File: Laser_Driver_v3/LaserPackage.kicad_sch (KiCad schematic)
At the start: 16 parts

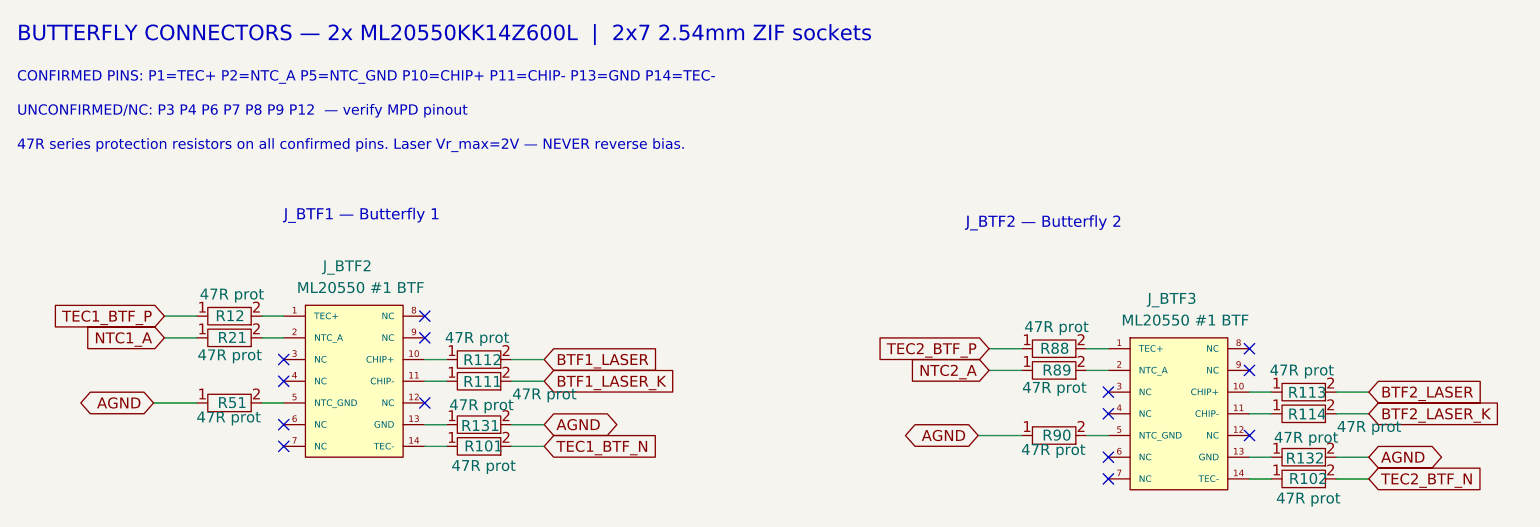
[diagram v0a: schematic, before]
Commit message: Renumbered schematics, corrections, power verified
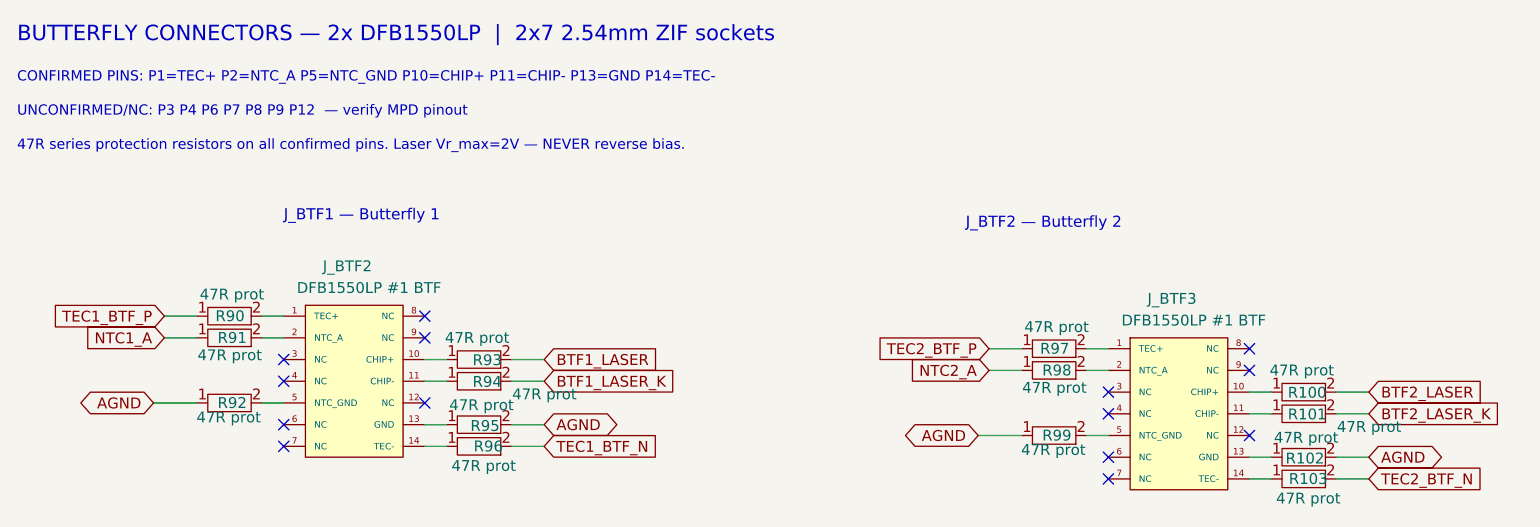
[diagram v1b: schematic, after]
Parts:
- J_BTF2, J_BTF3: value ML20550 #1 BTF -> DFB1550LP #1 BTF
- renumbered R113 to R100, R114 to R101, R132 to R102, R102 to R103, R12 to R90, R21 to R91, R51 to R92, R112 to R93, R111 to R94, R131 to R95, R101 to R96, R88 to R97, R89 to R98, R90 to R99
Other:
- note added: "BUTTERFLY CONNECTORS — 2x DFB1550LP | 2x7 2.54mm ZIF sockets"
- note removed: "BUTTERFLY CONNECTORS — 2x ML20550KK14Z600L | 2x7 2.54mm ZIF sockets"
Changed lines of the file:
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@@
 		)
 	)
-	(text "BUTTERFLY CONNECTORS — 2x ML20550KK14Z600L  |  2x7 2.54mm ZIF sockets"
+	(text "BUTTERFLY CONNECTORS — 2x DFB1550LP  |  2x7 2.54mm ZIF sockets"
 		(exclude_from_sim no)
 		(at 41.18 30.61 0)
@@
 			)
 		)
-		(property "Value" "ML20550 #1 BTF"
+		(property "Value" "DFB1550LP #1 BTF"
 			(at 170.434 64.008 0)
 			(show_name no)
@@
 		(in_pos_files yes)
 		(dnp no)
-		(property "Reference" "R113"
+		(property "Reference" "R100"
 			(at 194.438 72.456 90)
 			(show_name no)
@@
 			(project "laser_driver_v3"
 				(path "/b2c3d4e5-f6a7-8901-bcde-f12345678901/3cc9b630-4516-4d07-8624-99717cc6cbce"
-					(reference "R113")
+					(reference "R100")
 					(unit 1)
 				)
@@
 		(in_pos_files yes)
 		(dnp no)
-		(property "Reference" "R12"
+		(property "Reference" "R90"
 			(at 67.818 63.5 90)
 			(show_name no)
@@
 			(project "laser_driver_v3"
 				(path "/b2c3d4e5-f6a7-8901-bcde-f12345678901/3cc9b630-4516-4d07-8624-99717cc6cbce"
-					(reference "R12")
+					(reference "R90")
 					(unit 1)
 				)
@@
 		(in_pos_files yes)
 		(dnp no)
-		(property "Reference" "R132"
+		(property "Reference" "R102"
 			(at 194.184 80.156 90)
 			(show_name no)
@@
 			(project "laser_driver_v3"
 				(path "/b2c3d4e5-f6a7-8901-bcde-f12345678901/3cc9b630-4516-4d07-8624-99717cc6cbce"
-					(reference "R132")
+					(reference "R102")
 					(unit 1)
 				)
@@
 		(in_pos_files yes)
 		(dnp no)
-		(property "Reference" "R131"
+		(property "Reference" "R95"
 			(at 97.664 76.346 90)
 			(show_name no)
@@
 			(project "laser_driver_v3"
 				(path "/b2c3d4e5-f6a7-8901-bcde-f12345678901/3cc9b630-4516-4d07-8624-99717cc6cbce"
-					(reference "R131")
+					(reference "R95")
 					(unit 1)
 				)
@@
 		(in_pos_files yes)
 		(dnp no)
-		(property "Reference" "R21"
+		(property "Reference" "R91"
 			(at 68.072 66.04 90)
 			(show_name no)
@@
 			(project "laser_driver_v3"
 				(path "/b2c3d4e5-f6a7-8901-bcde-f12345678901/3cc9b630-4516-4d07-8624-99717cc6cbce"
-					(reference "R21")
+					(reference "R91")
 					(unit 1)
 				)
@@
 		(in_pos_files yes)
 		(dnp no)
-		(property "Reference" "R112"
+		(property "Reference" "R93"
 			(at 97.918 68.646 90)
 			(show_name no)
@@
 			(project "laser_driver_v3"
 				(path "/b2c3d4e5-f6a7-8901-bcde-f12345678901/3cc9b630-4516-4d07-8624-99717cc6cbce"
-					(reference "R112")
+					(reference "R93")
 					(unit 1)
 				)
@@
 		(in_pos_files yes)
 		(dnp no)
-		(property "Reference" "R88"
+		(property "Reference" "R97"
 			(at 164.338 67.31 90)
 			(show_name no)
@@
 			(project "laser_driver_v3"
 				(path "/b2c3d4e5-f6a7-8901-bcde-f12345678901/3cc9b630-4516-4d07-8624-99717cc6cbce"
-					(reference "R88")
+					(reference "R97")
 					(unit 1)
 				)
@@
 		(in_pos_files yes)
 		(dnp no)
-		(property "Reference" "R101"
+		(property "Reference" "R96"
 			(at 98.044 78.74 90)
 			(show_name no)
@@
 			(project "laser_driver_v3"
 				(path "/b2c3d4e5-f6a7-8901-bcde-f12345678901/3cc9b630-4516-4d07-8624-99717cc6cbce"
-					(reference "R101")
+					(reference "R96")
 					(unit 1)
 				)
@@
 		(in_pos_files yes)
 		(dnp no)
-		(property "Reference" "R114"
+		(property "Reference" "R101"
 			(at 194.438 74.996 90)
 			(show_name no)
@@
 			(project "laser_driver_v3"
 				(path "/b2c3d4e5-f6a7-8901-bcde-f12345678901/3cc9b630-4516-4d07-8624-99717cc6cbce"
-					(reference "R114")
+					(reference "R101")
 					(unit 1)
 				)
@@
 			)
 		)
-		(property "Value" "ML20550 #1 BTF"
+		(property "Value" "DFB1550LP #1 BTF"
 			(at 73.914 60.198 0)
 			(show_name no)
@@
 		(in_pos_files yes)
 		(dnp no)
-		(property "Reference" "R89"
+		(property "Reference" "R98"
 			(at 164.592 69.85 90)
 			(show_name no)
@@
 			(project "laser_driver_v3"
 				(path "/b2c3d4e5-f6a7-8901-bcde-f12345678901/3cc9b630-4516-4d07-8624-99717cc6cbce"
-					(reference "R89")
+					(reference "R98")
 					(unit 1)
 				)
@@
 		(in_pos_files yes)
 		(dnp no)
-		(property "Reference" "R90"
+		(property "Reference" "R99"
 			(at 164.592 77.47 90)
 			(show_name no)
@@
 			(project "laser_driver_v3"
 				(path "/b2c3d4e5-f6a7-8901-bcde-f12345678901/3cc9b630-4516-4d07-8624-99717cc6cbce"
-					(reference "R90")
+					(reference "R99")
 					(unit 1)
 				)
@@
 		(in_pos_files yes)
 		(dnp no)
-		(property "Reference" "R111"
+		(property "Reference" "R94"
 			(at 97.918 71.186 90)
 			(show_name no)
@@
 			(project "laser_driver_v3"
 				(path "/b2c3d4e5-f6a7-8901-bcde-f12345678901/3cc9b630-4516-4d07-8624-99717cc6cbce"
-					(reference "R111")
+					(reference "R94")
 					(unit 1)
 				)
@@
 		(in_pos_files yes)
 		(dnp no)
-		(property "Reference" "R102"
+		(property "Reference" "R103"
 			(at 194.564 82.55 90)
 			(show_name no)
@@
 			(project "laser_driver_v3"
 				(path "/b2c3d4e5-f6a7-8901-bcde-f12345678901/3cc9b630-4516-4d07-8624-99717cc6cbce"
-					(reference "R102")
+					(reference "R103")
 					(unit 1)
 				)
@@
 		(in_pos_files yes)
 		(dnp no)
-		(property "Reference" "R51"
+		(property "Reference" "R92"
 			(at 68.072 73.66 90)
 			(show_name no)
@@
 			(project "laser_driver_v3"
 				(path "/b2c3d4e5-f6a7-8901-bcde-f12345678901/3cc9b630-4516-4d07-8624-99717cc6cbce"
-					(reference "R51")
+					(reference "R92")
 					(unit 1)
 				)

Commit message: Update names, footprints, values, and created BOM
Updated files names, foot prints, component values, parts.
Assigned values from Digikey catalog.
Created CSV BOMs for each schematic.
Including a Power analysis now for all components.
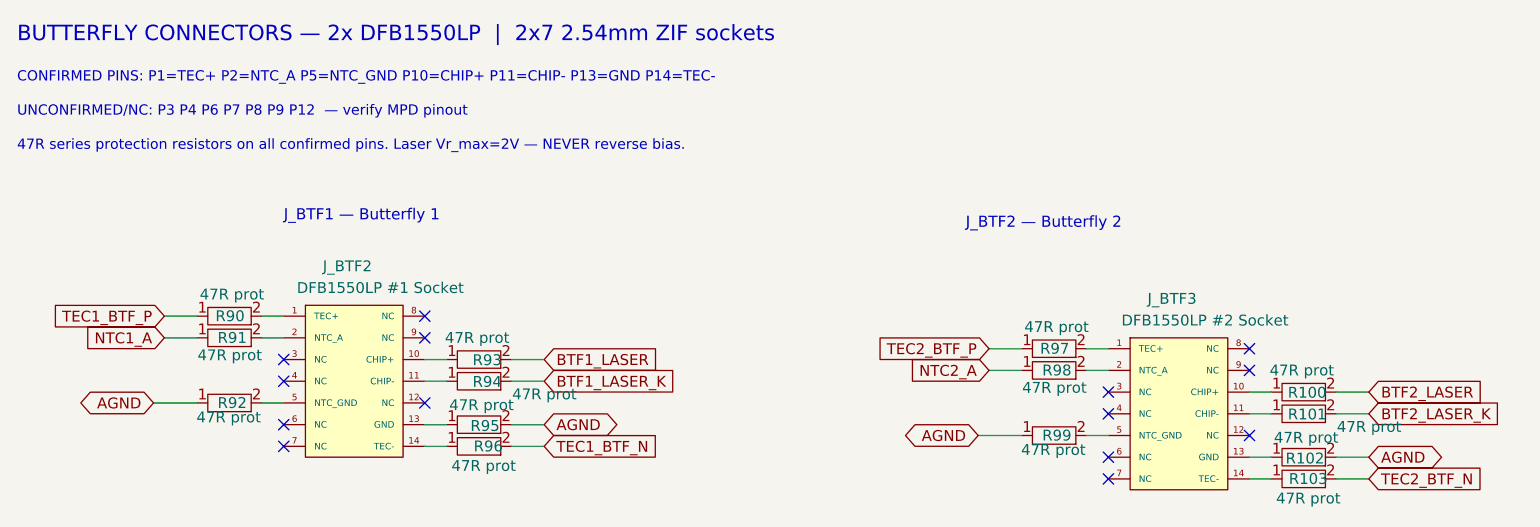
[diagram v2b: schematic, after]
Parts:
- J_BTF2: value DFB1550LP #1 BTF -> DFB1550LP #1 Socket; footprint Connector_PinHeader_2.54mm:PinHeader_2x07_P2.54mm_Vertical -> Connector_PinSocket_2.54mm:PinSocket_2x07_P2.54mm_Vertical
- J_BTF3: value DFB1550LP #1 BTF -> DFB1550LP #2 Socket; footprint Connector_PinHeader_2.54mm:PinHeader_2x07_P2.54mm_Vertical -> Connector_PinSocket_2.54mm:PinSocket_2x07_P2.54mm_Vertical
- R100, R101, R102, R103, R90, R91, R92, R93, R94, R95, R96, R97, R98, R99: footprint Resistor_SMD:R_0402_1005Metric -> Resistor_SMD:R_0805_2012Metric_Pad1.20x1.40mm_HandSolder
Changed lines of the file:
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@@
 			)
 		)
-		(property "Value" "DFB1550LP #1 BTF"
+		(property "Value" "DFB1550LP #2 Socket"
 			(at 170.434 64.008 0)
 			(show_name no)
@@
 			)
 		)
-		(property "Footprint" "Connector_PinHeader_2.54mm:PinHeader_2x07_P2.54mm_Vertical"
+		(property "Footprint" "Connector_PinSocket_2.54mm:PinSocket_2x07_P2.54mm_Vertical"
 			(at 180.594 85.598 0)
 			(hide yes)
@@
 			)
 		)
-		(property "Footprint" "Resistor_SMD:R_0402_1005Metric"
+		(property "Footprint" "Resistor_SMD:R_0805_2012Metric_Pad1.20x1.40mm_HandSolder"
 			(at 191.77 72.39 0)
 			(hide yes)
@@
 			)
 		)
-		(property "Footprint" "Resistor_SMD:R_0402_1005Metric"
+		(property "Footprint" "Resistor_SMD:R_0805_2012Metric_Pad1.20x1.40mm_HandSolder"
 			(at 66.04 63.5 0)
 			(hide yes)
@@
 			)
 		)
-		(property "Footprint" "Resistor_SMD:R_0402_1005Metric"
+		(property "Footprint" "Resistor_SMD:R_0805_2012Metric_Pad1.20x1.40mm_HandSolder"
 			(at 191.77 80.01 0)
 			(hide yes)
@@
 			)
 		)
-		(property "Footprint" "Resistor_SMD:R_0402_1005Metric"
+		(property "Footprint" "Resistor_SMD:R_0805_2012Metric_Pad1.20x1.40mm_HandSolder"
 			(at 95.25 76.2 0)
 			(hide yes)
@@
 			)
 		)
-		(property "Footprint" "Resistor_SMD:R_0402_1005Metric"
+		(property "Footprint" "Resistor_SMD:R_0805_2012Metric_Pad1.20x1.40mm_HandSolder"
 			(at 66.04 66.04 0)
 			(hide yes)
@@
 			)
 		)
-		(property "Footprint" "Resistor_SMD:R_0402_1005Metric"
+		(property "Footprint" "Resistor_SMD:R_0805_2012Metric_Pad1.20x1.40mm_HandSolder"
 			(at 95.25 68.58 0)
 			(hide yes)
@@
 			)
 		)
-		(property "Footprint" "Resistor_SMD:R_0402_1005Metric"
+		(property "Footprint" "Resistor_SMD:R_0805_2012Metric_Pad1.20x1.40mm_HandSolder"
 			(at 162.56 67.31 0)
 			(hide yes)
@@
 			)
 		)
-		(property "Footprint" "Resistor_SMD:R_0402_1005Metric"
+		(property "Footprint" "Resistor_SMD:R_0805_2012Metric_Pad1.20x1.40mm_HandSolder"
 			(at 95.25 78.74 0)
 			(hide yes)
@@
 			)
 		)
-		(property "Footprint" "Resistor_SMD:R_0402_1005Metric"
+		(property "Footprint" "Resistor_SMD:R_0805_2012Metric_Pad1.20x1.40mm_HandSolder"
 			(at 191.77 74.93 0)
 			(hide yes)
@@
 			)
 		)
-		(property "Value" "DFB1550LP #1 BTF"
+		(property "Value" "DFB1550LP #1 Socket"
 			(at 73.914 60.198 0)
 			(show_name no)
@@
 			)
 		)
-		(property "Footprint" "Connector_PinHeader_2.54mm:PinHeader_2x07_P2.54mm_Vertical"
+		(property "Footprint" "Connector_PinSocket_2.54mm:PinSocket_2x07_P2.54mm_Vertical"
 			(at 84.074 81.788 0)
 			(hide yes)
@@
 			)
 		)
-		(property "Footprint" "Resistor_SMD:R_0402_1005Metric"
+		(property "Footprint" "Resistor_SMD:R_0805_2012Metric_Pad1.20x1.40mm_HandSolder"
 			(at 162.56 69.85 0)
 			(hide yes)
@@
 			)
 		)
-		(property "Footprint" "Resistor_SMD:R_0402_1005Metric"
+		(property "Footprint" "Resistor_SMD:R_0805_2012Metric_Pad1.20x1.40mm_HandSolder"
 			(at 162.56 77.47 0)
 			(hide yes)
@@
 			)
 		)
-		(property "Footprint" "Resistor_SMD:R_0402_1005Metric"
+		(property "Footprint" "Resistor_SMD:R_0805_2012Metric_Pad1.20x1.40mm_HandSolder"
 			(at 95.25 71.12 0)
 			(hide yes)
@@
 			)
 		)
-		(property "Footprint" "Resistor_SMD:R_0402_1005Metric"
+		(property "Footprint" "Resistor_SMD:R_0805_2012Metric_Pad1.20x1.40mm_HandSolder"
 			(at 191.77 82.55 0)
 			(hide yes)
@@
 			)
 		)
-		(property "Footprint" "Resistor_SMD:R_0402_1005Metric"
+		(property "Footprint" "Resistor_SMD:R_0805_2012Metric_Pad1.20x1.40mm_HandSolder"
 			(at 66.04 73.66 0)
 			(hide yes)

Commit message: first placement of all components on pcb.
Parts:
- removed J_BTF2: DFB1550LP #1 Socket, Connector_PinSocket_2.54mm:PinSocket_2x07_P2.54mm_Vertical, symbol Connector:Conn_02x07_Odd_Even
- removed J_BTF3: DFB1550LP #2 Socket, Connector_PinSocket_2.54mm:PinSocket_2x07_P2.54mm_Vertical, symbol Connector:Conn_02x07_Odd_Even
- removed R100, R101, R102, R103, R90, R91, R92, R93, R94, R95, R96, R97, R98, R99: 47R prot, Resistor_SMD:R_0805_2012Metric_Pad1.20x1.40mm_HandSolder, symbol Device:R
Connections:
- no-connect marks 14 -> 0
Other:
- note removed: "47R series protection resistors on all confirmed pins. Laser Vr_max=2V — NEVER reverse bias."
- note removed: "BUTTERFLY CONNECTORS — 2x DFB1550LP | 2x7 2.54mm ZIF sockets"
- note removed: "CONFIRMED PINS: P1=TEC+ P2=NTC_A P5=NTC_GND P10=CHIP+ P11=CHIP- P13=GND P14=TEC-"
- note removed: "J_BTF1 — Butterfly 1"
- note removed: "J_BTF2 — Butterfly 2"
- note removed: "UNCONFIRMED/NC: P3 P4 P6 P7 P8 P9 P12 — verify MPD pinout"
